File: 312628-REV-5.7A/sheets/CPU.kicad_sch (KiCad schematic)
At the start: 57 parts, among them CN101 SPEAKER, CN102 KEYBRD, J1 ALEBODGE_LEFT, Q101 2N3904, U1 74LS04, U101 FE2010, U102 8088, U103 8087, U104 74LS245, U105 74LS373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

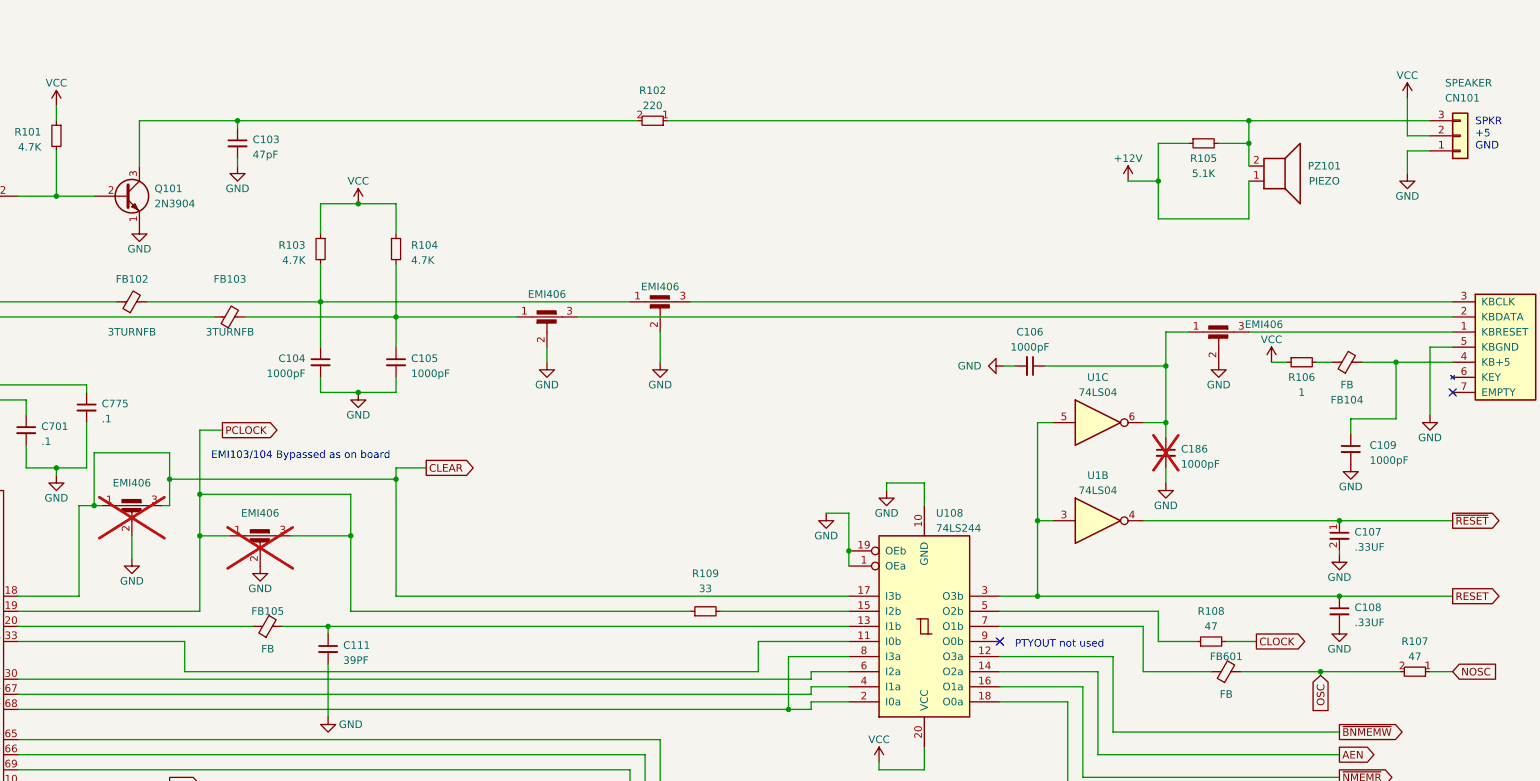
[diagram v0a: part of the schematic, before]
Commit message: update schematics to kicad 7.0.8
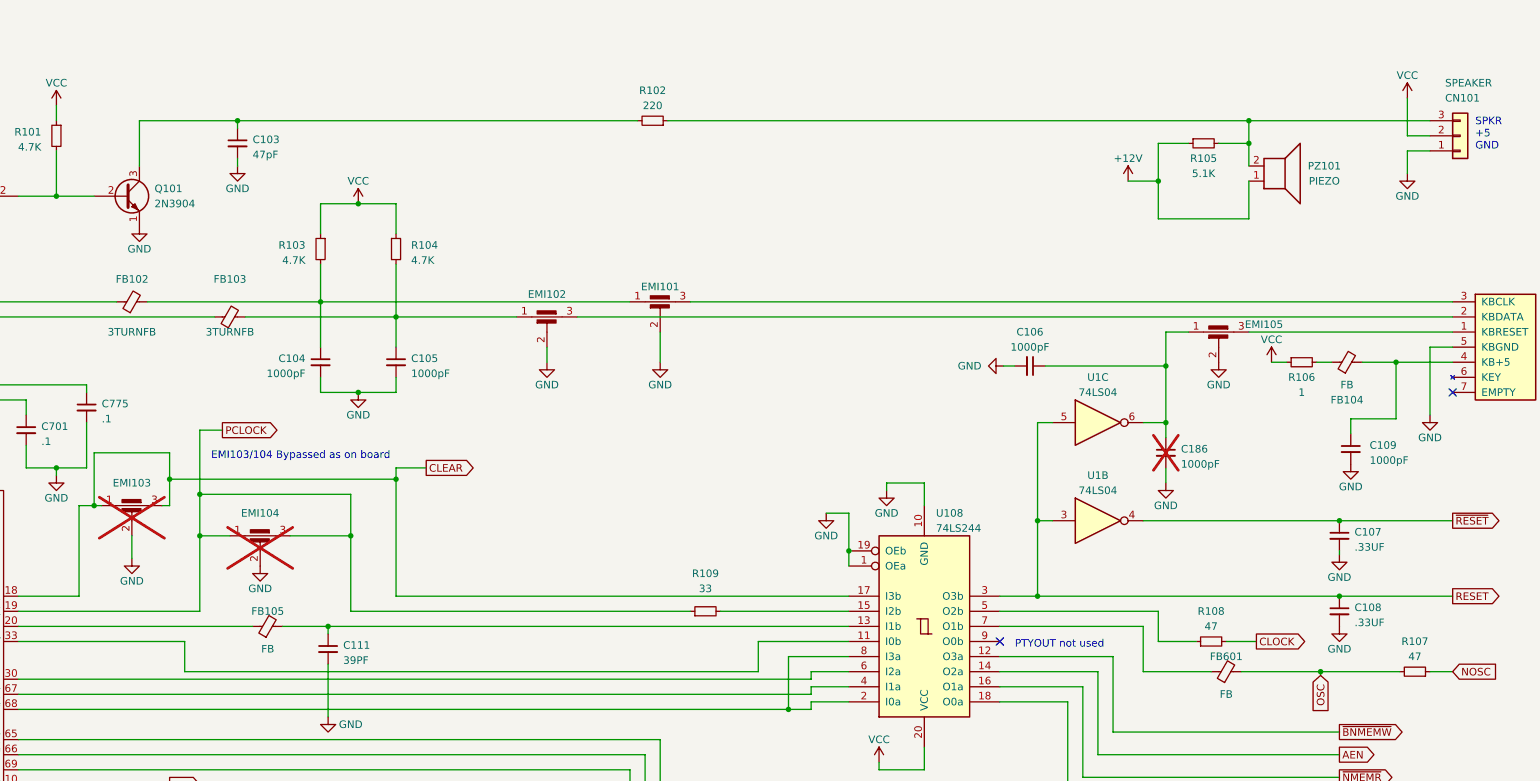
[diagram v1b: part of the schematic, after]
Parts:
- renumbered EMI406 to EMI101, EMI406 to EMI102, EMI406 to EMI103, EMI406 to EMI104, EMI406 to EMI105
